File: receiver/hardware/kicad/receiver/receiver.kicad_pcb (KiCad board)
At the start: 2 copper layers, 27 parts, among them J1 Connector, U1 74HC595, U2 74HC595

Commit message: Initial layout
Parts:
- D1, D2, D4, D5, D7: footprint LED_THT:LED_D5.0mm-4_RGB_Wide_Pins -> LED_THT:LED_D5.0mm-4_RGB_Staggered_Pins
- R10, R12, R13, R15, R16, R18, R19, R2, R21, R23, R25, R4, R7, R9: moved to B.Cu
- moved C1 131.7 mm to (146.5, 137.2), turned to 180 degrees
- moved C2 130.3 mm to (156.8, 137.2), turned to 180 degrees
- moved R19 112.9 mm to (156.2, 107.2)
- moved R7 111.0 mm to (156.2, 93.8)
- moved R16 108.4 mm to (156.2, 104.0)
- moved R10 105.2 mm to (156.2, 97.2)
- moved R13 104.4 mm to (147.5, 107.5), turned to 180 degrees
- moved R2 103.3 mm to (153.5, 58.8), turned to 270 degrees
- moved R18 102.6 mm to (156.2, 77.0)
- moved R23 100.9 mm to (156.2, 83.8)
- moved R4 100.9 mm to (147.5, 97.2), turned to 180 degrees
- moved R25 96.8 mm to (156.2, 87.0)
- moved R12 96.8 mm to (147.5, 76.8), turned to 180 degrees
- moved R15 93.1 mm to (156.2, 73.5)
- moved R21 89.9 mm to (147.5, 87.0), turned to 180 degrees
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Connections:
- R25 pad 2: (no net) -> Net-(R25-Pad2)
- U2 pad 1: Net-(R7-Pad2) -> Net-(R4-Pad2)
- U2 pad 15: Net-(R4-Pad2) -> Net-(R25-Pad2)
- U2 pad 2: Net-(R10-Pad2) -> Net-(R7-Pad2)
- U2 pad 3: Net-(R13-Pad2) -> Net-(R10-Pad2)
- U2 pad 4: Net-(R16-Pad2) -> Net-(R13-Pad2)
- U2 pad 5: Net-(R19-Pad2) -> Net-(R16-Pad2)
- U2 pad 6: (no net) -> Net-(R19-Pad2)

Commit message: Wired
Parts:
- C1, C2, J1, U1, U2: moved to B.Cu
- D1, D2, D4, D5, D7: footprint LED_THT:LED_D5.0mm-4_RGB_Staggered_Pins -> LED_THT:LED_D5.0mm-4_RGB
- moved C1 63.7 mm to (141.8, 73.8), turned to 90 degrees
- moved U1 52.0 mm to (144.8, 78.7), turned to 180 degrees
- moved C2 45.8 mm to (141.8, 94.0), turned to 90 degrees
- moved U2 33.8 mm to (144.8, 99.1), turned to 180 degrees
- moved J1 17.0 mm to (143.0, 114.2)
- moved R3 9.25 mm to (156.2, 63.8), turned to 0 degrees
- moved R12 9.17 mm to (156.2, 74.0), turned to 0 degrees
- moved R21 9.17 mm to (156.2, 84.2), turned to 0 degrees
- moved R4 9.17 mm to (156.2, 94.5), turned to 0 degrees
- moved R13 8.93 mm to (156.0, 104.8), turned to 0 degrees
- moved R16 3.51 mm to (156.0, 107.5)
- moved R7 3.50 mm to (156.2, 97.2)
- moved R15 3.25 mm to (156.2, 76.8)
- moved R23 3.25 mm to (156.2, 87.0)
- moved R6 3.25 mm to (156.2, 66.5)
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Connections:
- D1 pad 1: GND -> Net-(D1-Pad1)
- D1 pad 2: Net-(D1-Pad2) -> GND
- D2 pad 1: GND -> Net-(D2-Pad1)
- D2 pad 2: Net-(D2-Pad2) -> GND
- D4 pad 1: GND -> Net-(D4-Pad1)
- D4 pad 2: Net-(D4-Pad2) -> GND
- D5 pad 1: GND -> Net-(D5-Pad1)
- D5 pad 2: Net-(D5-Pad2) -> GND
- D7 pad 1: GND -> Net-(D7-Pad1)
- D7 pad 2: Net-(D7-Pad2) -> GND
- R12 pad 1: Net-(D4-Pad2) -> Net-(D4-Pad1)
- R13 pad 1: Net-(D5-Pad2) -> Net-(D5-Pad1)
- R21 pad 1: Net-(D7-Pad2) -> Net-(D7-Pad1)
- R3 pad 1: Net-(D1-Pad2) -> Net-(D1-Pad1)
- R4 pad 1: Net-(D2-Pad2) -> Net-(D2-Pad1)
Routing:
- net +3V3: track 0.00 -> 79.3 mm
- net GND: track 0.00 -> 77.3 mm, vias 0 -> 2
- net LDR: track 0.00 -> 64.6 mm, vias 0 -> 1
- net CLOCK: track 0.00 -> 50.0 mm, vias 0 -> 4
- net LATCH: track 0.00 -> 48.5 mm, vias 0 -> 4
- net DATA: track 0.00 -> 41.4 mm, vias 0 -> 1
- net Net-(R3-Pad2): track 0.00 -> 26.4 mm, vias 0 -> 2
- net Net-(R19-Pad2): track 0.00 -> 23.1 mm, vias 0 -> 2
- net Net-(R16-Pad2): track 0.00 -> 22.0 mm, vias 0 -> 2
- net Net-(R23-Pad2): track 0.00 -> 21.1 mm, vias 0 -> 2
- net Net-(U1-Pad9): track 0.00 -> 20.7 mm, vias 0 -> 2
- net Net-(R25-Pad2): track 0.00 -> 20.7 mm, vias 0 -> 2
- net Net-(R9-Pad2): track 0.00 -> 20.4 mm, vias 0 -> 2
- net Net-(R6-Pad2): track 0.00 -> 20.2 mm, vias 0 -> 2
- net Net-(R13-Pad2): track 0.00 -> 11.6 mm
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- added copper zone on B.Cu, net +3V3
- added copper zone on B.Cu, net GND
- added copper zone on F.Cu, net GND
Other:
- board outline added: 25 x 64 mm
- net class 3V3 added: clearance 0.25, trace_width 0.5, via_dia 0.8, via_drill 0.4

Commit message: Resizing
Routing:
- net DATA: track 41.4 -> 44.9 mm
- net GND: track 77.3 -> 78.0 mm
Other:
- board size 25 x 64 mm -> 22 x 64 mm
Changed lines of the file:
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@@
     (thickness 1.6)
     (drawings 9)
-    (tracks 308)
+    (tracks 313)
     (zones 0)
     (modules 27)
@@
     (39 F.Mask user)
     (40 Dwgs.User user)
-    (41 Cmts.User user hide)
+    (41 Cmts.User user)
     (42 Eco1.User user)
     (43 Eco2.User user)
@@
   )
   (gr_line (start 138 54) (end 138 118) (layer Edge.Cuts) (width 0.15))
-  (gr_line (start 163 54) (end 138 54) (layer Edge.Cuts) (width 0.15))
-  (gr_line (start 163 118) (end 163 54) (layer Edge.Cuts) (width 0.15))
-  (gr_line (start 138 118) (end 163 118) (layer Edge.Cuts) (width 0.15))
+  (gr_line (start 160 54) (end 138 54) (layer Edge.Cuts) (width 0.15))
+  (gr_line (start 160 118) (end 160 54) (layer Edge.Cuts) (width 0.15))
+  (gr_line (start 138 118) (end 160 118) (layer Edge.Cuts) (width 0.15))
   (dimension 25 (width 0.3) (layer Cmts.User)
     (gr_text "25.000 mm" (at 150.5 133.1) (layer Cmts.User)
@@
   (segment (start 140.295 98.735) (end 140.29 98.73) (width 0.25) (layer B.Cu) (net 1))
   (segment (start 141.83 98.735) (end 140.295 98.735) (width 0.25) (layer B.Cu) (net 1))
-  (segment (start 140.29 109) (end 145.54 114.25) (width 0.25) (layer F.Cu) (net 1))
-  (segment (start 140.29 98.73) (end 140.29 109) (width 0.25) (layer F.Cu) (net 1))
   (segment (start 149.42 92.39) (end 149.86 92.83) (width 0.25) (layer B.Cu) (net 1))
   (segment (start 146.92 92.79) (end 147.32 92.39) (width 0.25) (layer B.Cu) (net 1))
@@
   (segment (start 144.9 71.75) (end 149.25 71.75) (width 0.25) (layer B.Cu) (net 1))
   (segment (start 142.875 71.75) (end 144.9 71.75) (width 0.25) (layer B.Cu) (net 1))
+  (segment (start 144.690001 113.400001) (end 145.54 114.25) (width 0.25) (layer F.Cu) (net 1))
+  (segment (start 140.29 110.30641) (end 142.65359 112.67) (width 0.25) (layer F.Cu) (net 1))
+  (segment (start 140.29 98.73) (end 140.29 110.30641) (width 0.25) (layer F.Cu) (net 1))
+  (segment (start 142.65359 112.67) (end 143.96 112.67) (width 0.25) (layer F.Cu) (net 1))
+  (segment (start 143.96 112.67) (end 144.690001 113.400001) (width 0.25) (layer F.Cu) (net 1))
   (segment (start 139.75 60.75) (end 143.75 56.75) (width 0.5) (layer B.Cu) (net 2))
   (segment (start 141.75 74.625) (end 139.875 74.625) (width 0.5) (layer B.Cu) (net 2))
@@
   (segment (start 151.13 83.82) (end 151.13 86.93) (width 0.25) (layer F.Cu) (net 12))
   (segment (start 151.2 87) (end 155.375 87) (width 0.25) (layer B.Cu) (net 12))
-  (segment (start 148.08 114.25) (end 147 113.17) (width 0.25) (layer F.Cu) (net 13))
   (segment (start 143.600001 77.399999) (end 144 77) (width 0.25) (layer B.Cu) (net 13))
-  (segment (start 147 80) (end 144.399999 77.399999) (width 0.25) (layer F.Cu) (net 13))
-  (segment (start 144.399999 77.399999) (end 144 77) (width 0.25) (layer F.Cu) (net 13))
   (via (at 144 77) (size 0.8) (drill 0.4) (layers F.Cu B.Cu) (net 13))
-  (segment (start 147 113.17) (end 147 80) (width 0.25) (layer F.Cu) (net 13))
   (segment (start 143.235 77.765) (end 143.600001 77.399999) (width 0.25) (layer B.Cu) (net 13))
   (segment (start 141.83 77.765) (end 143.235 77.765) (width 0.25) (layer B.Cu) (net 13))
+  (segment (start 147.230001 113.400001) (end 148.08 114.25) (width 0.25) (layer F.Cu) (net 13))
+  (segment (start 145.87 112.04) (end 147.230001 113.400001) (width 0.25) (layer F.Cu) (net 13))
+  (segment (start 144 77) (end 141.824999 79.175001) (width 0.25) (layer F.Cu) (net 13))
+  (segment (start 143.08 112.04) (end 145.87 112.04) (width 0.25) (layer F.Cu) (net 13))
+  (segment (start 141.824999 79.175001) (end 141.824999 110.784999) (width 0.25) (layer F.Cu) (net 13))
+  (segment (start 141.824999 110.784999) (end 143.08 112.04) (width 0.25) (layer F.Cu) (net 13))
   (via (at 144.6 110.4) (size 0.8) (drill 0.4) (layers F.Cu B.Cu) (net 14))
   (via (at 150.58 110.369998) (size 0.8) (drill 0.4) (layers F.Cu B.Cu) (net 14))

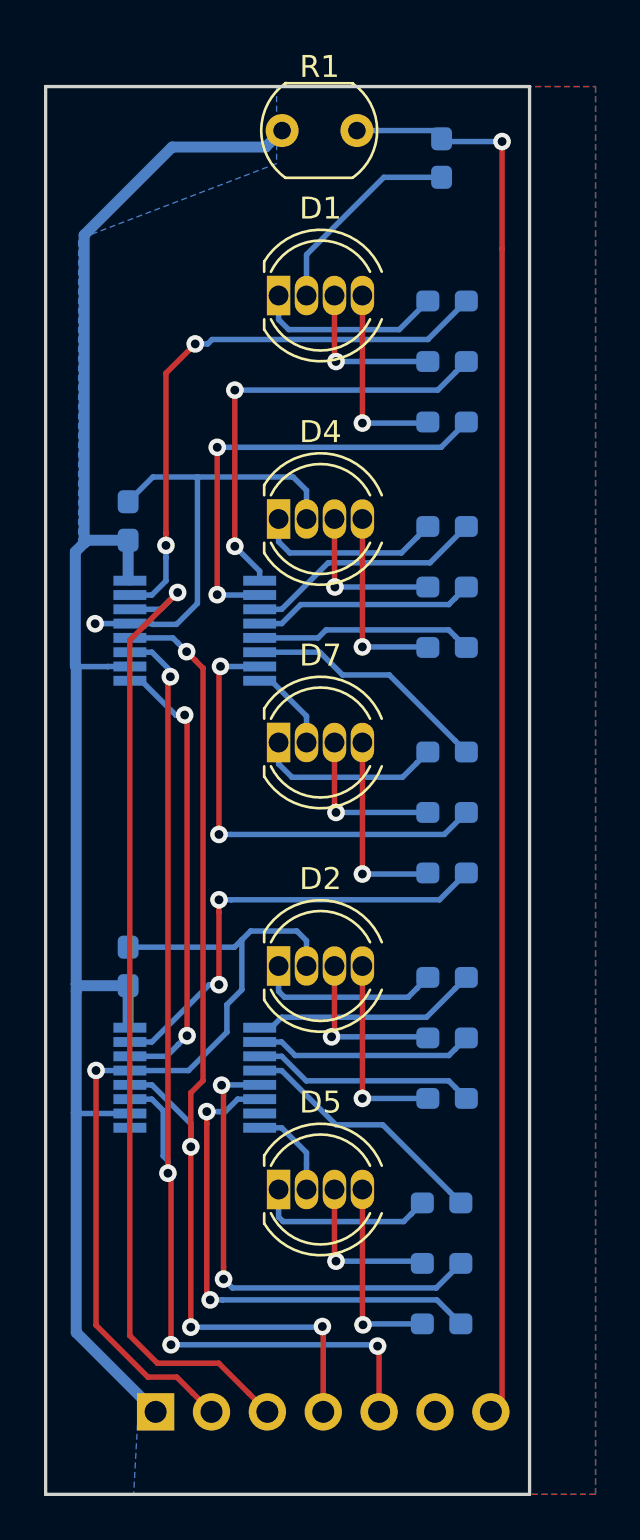
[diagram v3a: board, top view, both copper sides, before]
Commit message: Fit beneath the NodeMCU
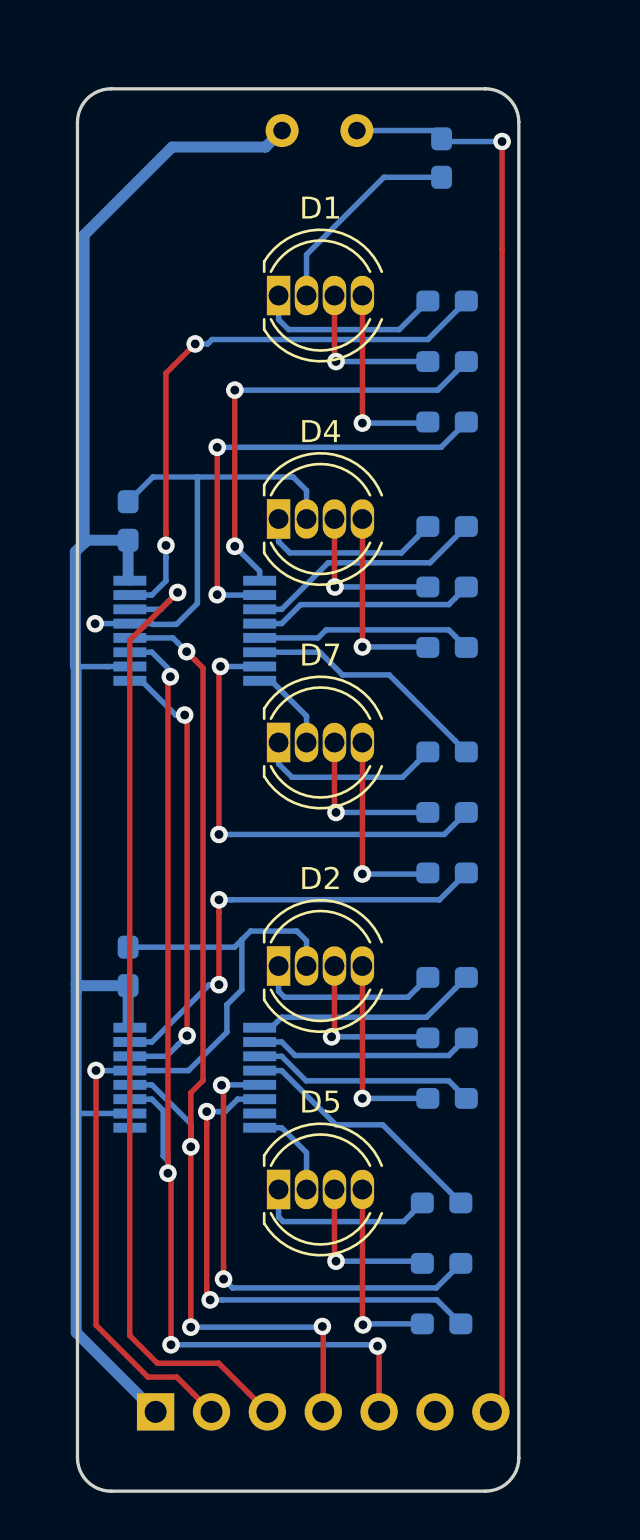
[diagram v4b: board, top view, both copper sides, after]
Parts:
- R1: moved to B.Cu
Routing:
- removed copper zone on B.Cu, net +3V3
- removed copper zone on B.Cu, net GND
- removed copper zone on F.Cu, net GND
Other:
- board size 22 x 64 mm -> 20.1 x 63.8 mm
- rule pad_to_mask_clearance: 0.051 -> 0

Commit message: Wired
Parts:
- moved U2 1.72 mm to (146.5, 99.0)
- moved U1 1.62 mm to (146.4, 78.7)
- moved C2 1.46 mm to (143.0, 94.7), turned to 0 degrees
- moved C1 1.26 mm to (143.0, 73.7), turned to 0 degrees
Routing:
- net GND: track 78.0 -> 49.9 mm, vias 2 -> 4
- net +3V3: track 79.3 -> 84.8 mm
- net Net-(U1-Pad9): track 20.7 -> 23.8 mm
- net CLOCK: track 50.0 -> 47.8 mm
- net DATA: track 44.9 -> 42.9 mm
- net Net-(R23-Pad2): track 21.1 -> 19.3 mm
- net Net-(R4-Pad2): track 10.3 -> 8.62 mm
- net Net-(R15-Pad2): track 10.1 -> 8.45 mm
- net Net-(R18-Pad2): track 9.88 -> 8.24 mm
- net Net-(R21-Pad2): track 11.3 -> 9.67 mm
- net Net-(R10-Pad2): track 10.2 -> 8.61 mm
- net Net-(R7-Pad2): track 9.98 -> 8.43 mm
- net Net-(R16-Pad2): track 22.0 -> 20.6 mm
- net Net-(R25-Pad2): track 20.7 -> 19.8 mm
- net Net-(R3-Pad2): track 26.4 -> 25.5 mm
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- added copper zone on B.Cu, net +3V3
- added copper zone on B.Cu, net GND
- added copper zone on F.Cu, net GND
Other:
- board text added: "https://github.com/theapi/esp8266wsn v2.0.0 Jan 2020"

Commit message: Logos
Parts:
- added REF**: TheApiLogoTiny, theapi:TheApiLogoTiny, F.Cu at (142.7, 56.8)
- added REF**: TheApiLogoTiny, theapi:TheApiLogoTiny, B.Cu at (142.7, 56.8)
- moved C1 1.27 mm to (141.7, 73.7)
- moved C2 1.27 mm to (141.7, 94.7)
- moved D1 1.27 mm to (147.3, 63.5)
- moved D2 1.27 mm to (147.3, 94.0)
- moved D4 1.27 mm to (147.3, 73.7)
- moved D5 1.27 mm to (147.3, 104.1)
- moved D7 1.27 mm to (147.3, 83.8)
- moved J1 1.27 mm to (141.7, 114.2)
- moved R1 1.27 mm to (147.5, 56.0)
- moved R10 1.27 mm to (155.0, 100.0)
- moved R12 1.27 mm to (155.0, 74.0)
- moved R13 1.27 mm to (154.7, 104.8)
- moved R15 1.27 mm to (155.0, 76.8)
- moved R16 1.27 mm to (154.7, 107.5)
- moved R18 1.27 mm to (155.0, 79.5)
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
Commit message: Labels
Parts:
- moved R2 1.22 mm to (154.9, 56.0), turned to 0 degrees
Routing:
- net GND: track 49.9 -> 47.3 mm
- net LDR: track 63.9 -> 62.9 mm
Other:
- board text added: "3V3"
- board text added: "CLK"
- board text added: "D"
- board text added: "GND"
- board text added: "LDR"
- board text added: "LT"
